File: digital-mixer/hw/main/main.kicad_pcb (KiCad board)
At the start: 2 copper layers, 114 x 112.5 mm, 184 parts, among them J1 GCT USB4085, J10 MIDI OUT SJ-43514-SMT, J2 LiPo 1S 3000 mAh (з платою за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, J3 IN1 SJ-43514-SMT, J4 IN2 SJ-43514-SMT, J5 IN3 SJ-43514-SMT, J6 IN4 SJ-43514-SMT, J7 MAIN OUT SJ-43514-SMT, J8 AUX OUT SJ-43514-SMT, J9 PHONES SJ-43514-SMT, Q1 AO3401A, SW1 Power 7x7 DPDT self-lock, SW10 EC11 ch3.1, SW11 EC11 ch3.2, SW12 EC11 ch3.3, SW13 Mute 3 TSF-1266, SW14 EC11 ch4.1, SW15 EC11 ch4.2, SW16 EC11 ch4.3, SW17 Mute 4 TSF-1266, SW18 EC11 master, SW19 FX1 TSF-1266, SW2 EC11 ch1.1, SW20 FX2 TSF-1266, SW21 AUX TSF-1266, SW22 CUE TSF-1266, SW23 SHIFT TSF-1266, SW3 EC11 ch1.2, SW4 EC11 ch1.3, SW5 Mute 1 TSF-1266, SW6 EC11 ch2.1, SW7 EC11 ch2.2, SW8 EC11 ch2.3, SW9 Mute 2 TSF-1266, U1 Teensy 4.1, U10 PCM5102A, U11 TPA6132A2, U12 MCP23017-E/SO, U13 MCP23017-E/SO, U2 USBLC6-2SC6, U3 TP4056, U4 TPS63802, U5 LP5907MFX-3.3, U6 PCM1865, U7 PCM1865, U8 PCM5102A, U9 PCM5102A

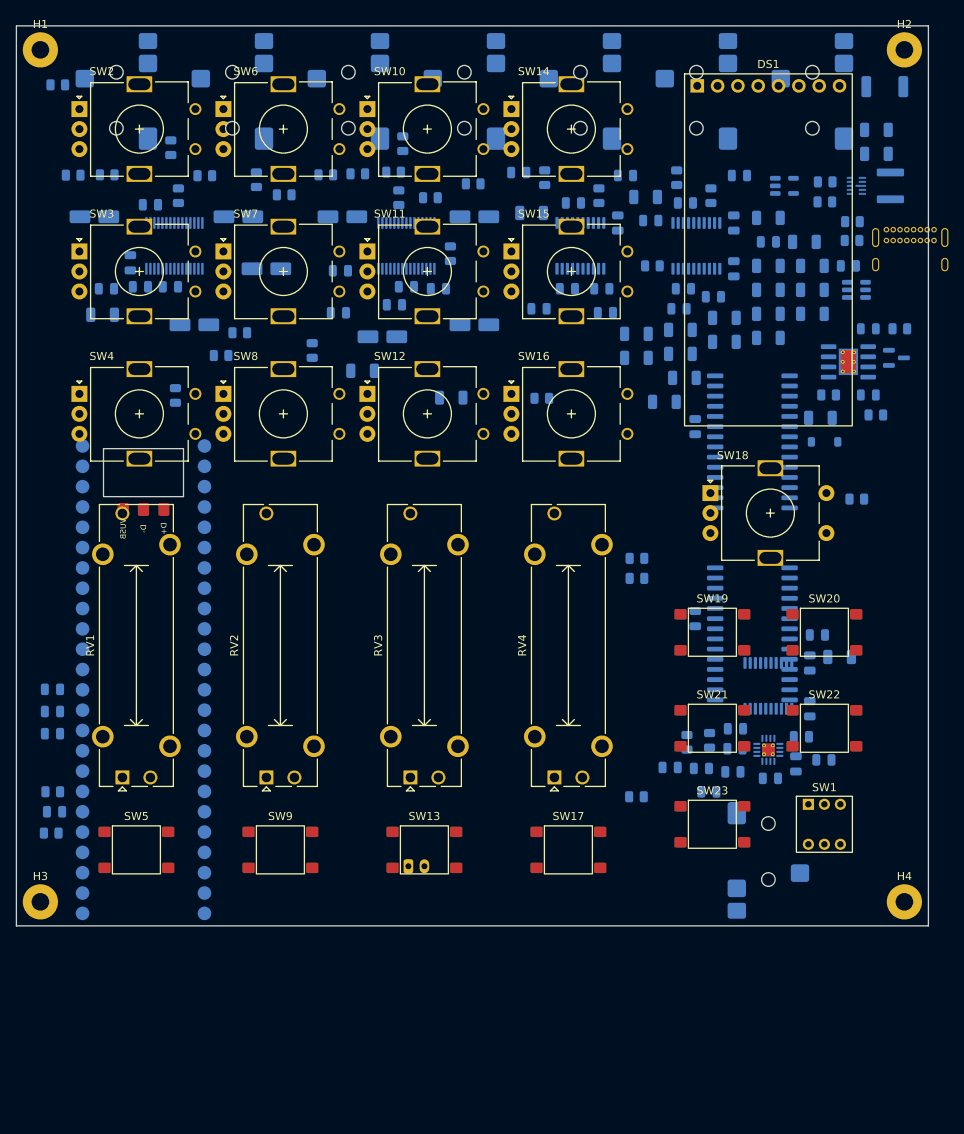
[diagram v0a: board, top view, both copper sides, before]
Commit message: digital-mixer: компоновка A (DM24), footprint за кресленнями GMT147, TSF-1266, кнопки 7x7
- розстановка: джеки ззаду, Teensy під Mute (microSD ліворуч), електроніка під правою колонкою,
  M2 у кутах; DRC розстановки: без перетинів корпусів і замикань
- route_pcb.py / fix_pcb.py для 2 шарів (з Rev A)

Co-Authored-By: Claude Opus 5.5 <noreply@anthropic.com>
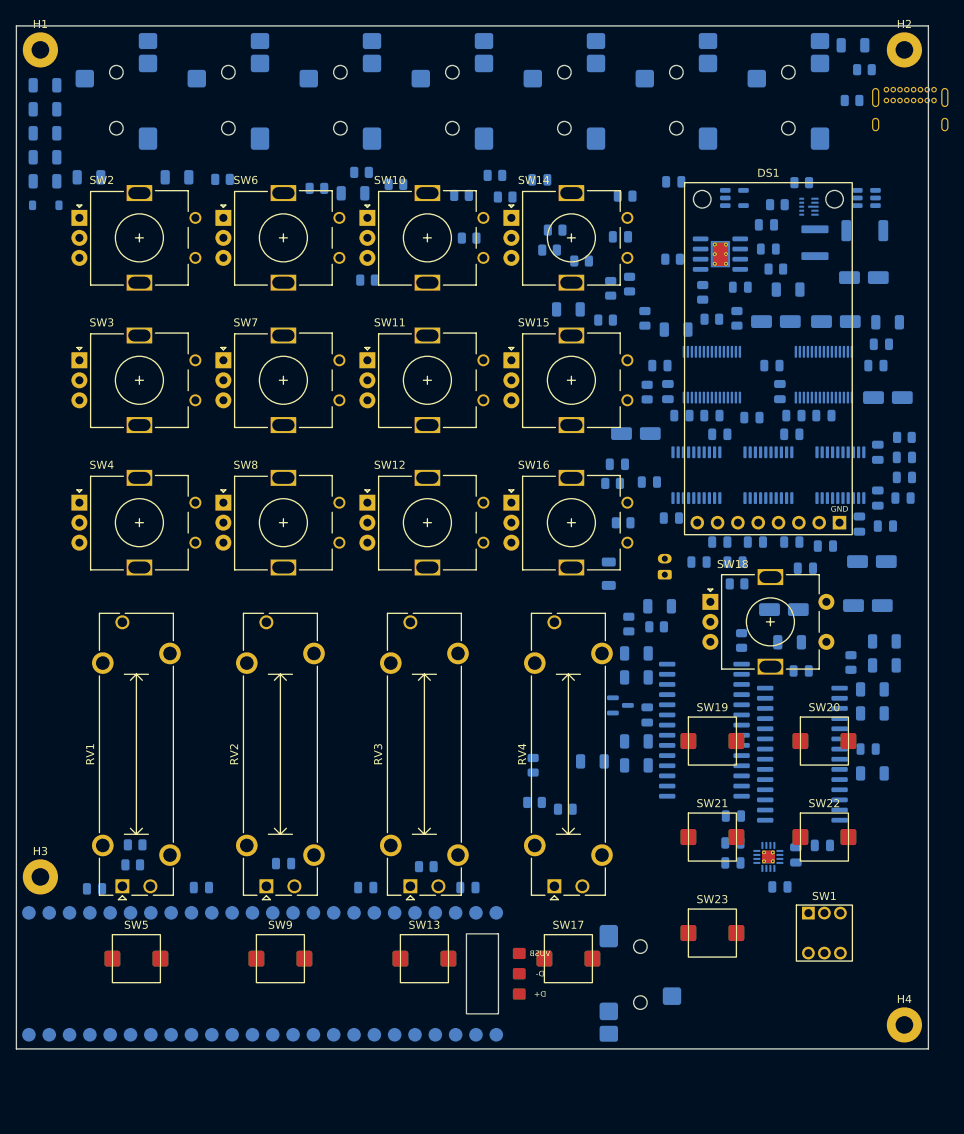
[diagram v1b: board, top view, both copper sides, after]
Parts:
- moved C80 118.2 mm to (76.4, 127.7)
- moved C64 103.9 mm to (23.6, 36.4)
- moved D3 101.7 mm to (23.7, 42.4)
- moved C15 101.7 mm to (128.9, 66.5)
- moved C7 96.2 mm to (29.1, 38.9)
- moved C6 86.7 mm to (23.6, 30.4)
- moved C53 86.2 mm to (23.6, 27.4)
- moved C81 82.2 mm to (23.6, 39.4)
- moved C16 79.8 mm to (111.9, 69.0)
- moved C63 78.1 mm to (23.6, 33.4)
- moved C27 73.9 mm to (115.9, 93.0)
- moved C12 72.7 mm to (114.9, 57.0)
- moved C20 71.7 mm to (102.5, 58.0)
- moved C14 71.5 mm to (122.4, 57.0)
- moved C19 69.9 mm to (100.4, 62.5)
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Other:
- board size 114 x 112.5 mm -> 114 x 127.9 mm

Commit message: digital-mixer: двошарова плата розведена (DRC: 0 розривів, 0 порушень по міді)
- Teensy праворуч спереду (microSD у правий торець), USB-C і PHONES на фронті: USB D+/D- ~30 мм
- блок TPS63802 за прикладом TI, доріжки зафіксовані; конденсатори біля виводів
- footprint TSF-1266 без подвійного courtyard; route_pcb зберігає зафіксовані доріжки
- docs/04-pcb.md

Co-Authored-By: Claude Opus 5.5 <noreply@anthropic.com>
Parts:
- U11: footprint Package_DFN_QFN:WQFN-16-1EP_3x3mm_P0.5mm_EP1.6x1.6mm_ThermalVias -> Package_DFN_QFN:WQFN-16-1EP_3x3mm_P0.5mm_EP1.6x1.6mm
- U3: footprint Package_SO:SOIC-8-1EP_3.9x4.9mm_P1.27mm_EP2.41x3.3mm_ThermalVias -> Package_SO:SOIC-8-1EP_3.9x4.9mm_P1.27mm_EP2.41x3.3mm
- moved J1 131.3 mm to (69.2, 141.8)
- moved R9 131.1 mm to (61.0, 139.3)
- moved R10 124.9 mm to (65.0, 139.1)
- moved U2 110.1 mm to (66.2, 133.8)
- moved C6 103.0 mm to (86.5, 111.9)
- moved C81 102.4 mm to (124.6, 22.4)
- moved C52 95.3 mm to (92.0, 111.9)
- moved C7 95.2 mm to (122.5, 57.2)
- moved C3 90.0 mm to (119.7, 128.1)
- moved R8 86.1 mm to (120.9, 125.1)
- moved C8 83.1 mm to (122.5, 49.0)
- moved R7 76.8 mm to (111.3, 128.1)
- moved C53 72.1 mm to (90.0, 55.4)
- moved C63 65.5 mm to (84.5, 57.4)
- moved C64 63.5 mm to (84.5, 54.4)
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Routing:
- net /+4V2: track 0.00 -> 5.90 mm
- net /BB_L1: track 0.00 -> 4.27 mm
- net /BB_L2: track 0.00 -> 4.23 mm
- net /VSYS: track 0.00 -> 3.35 mm

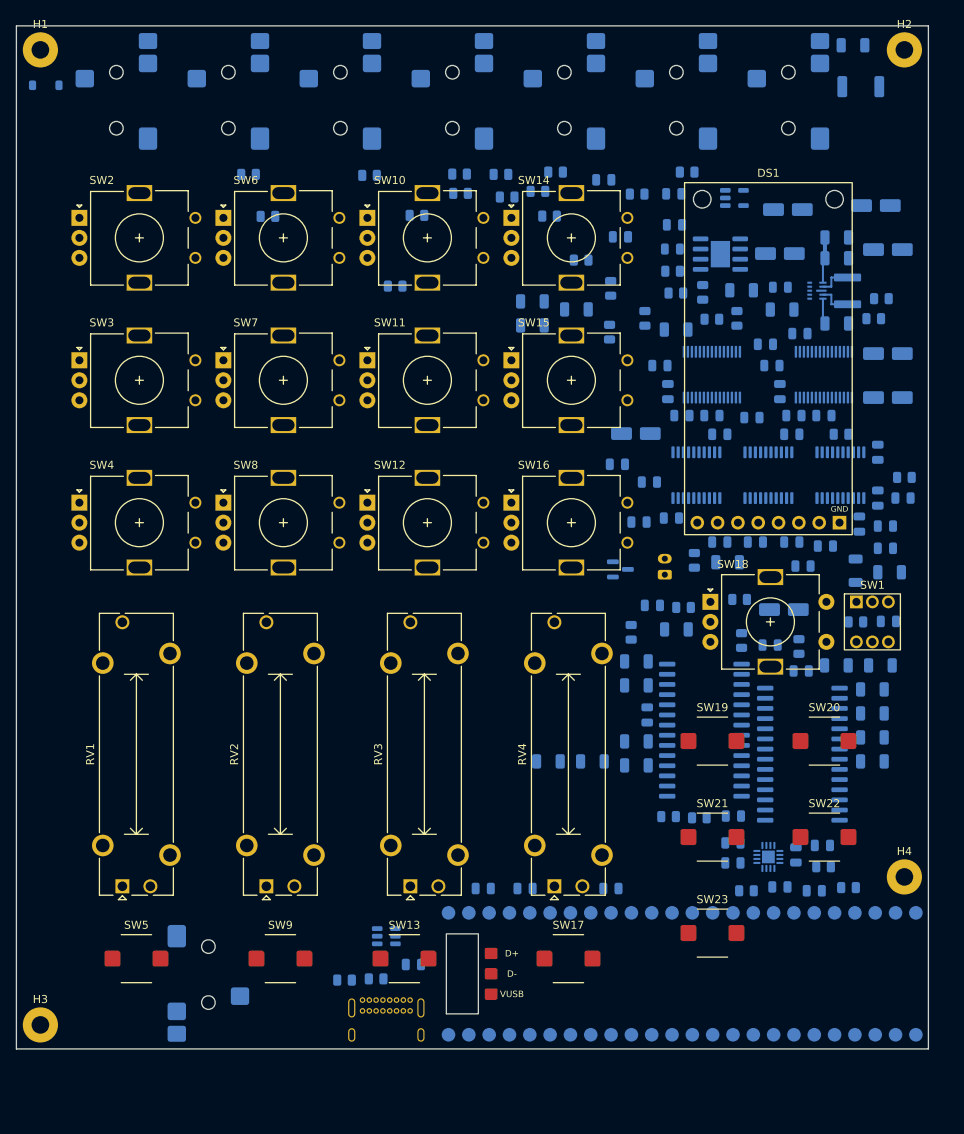
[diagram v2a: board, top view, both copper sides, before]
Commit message: digital-mixer: компоновка C (DM25-DM30), SMD-енкодери, USB4110, розводка 0 помилок
- компоновка C: колонки каналів на одних осях, ON / дисплей / MASTER в один ряд,
  Teensy у передньому правому куті, виходи на правому торці, M2 у чотирьох кутах
- EC12SY SMD з кнопками (DM26) + третій MCP23017; кнопку CUE прибрано (DM28)
- кнопка живлення 5,8 мм SMD (DM27), USB-C GCT USB4110 SMD (DM30), JST PH SMD
- 33 Ω на тактах I2S / TDM (DM29); такти 60-73 мм замість ~110
- 3D-моделі для всіх власних і стокових footprint без моделі (hw/lib/gen_3d.py)
- common: route_pcb --hole-keep, rip_near.py, параметри проєкту в kisch
- DRC: 0 порушень, 0 нез'єднаних, 0 розбіжностей зі схемою; ERC 0

Co-Authored-By: Claude Opus 5.5 <noreply@anthropic.com>
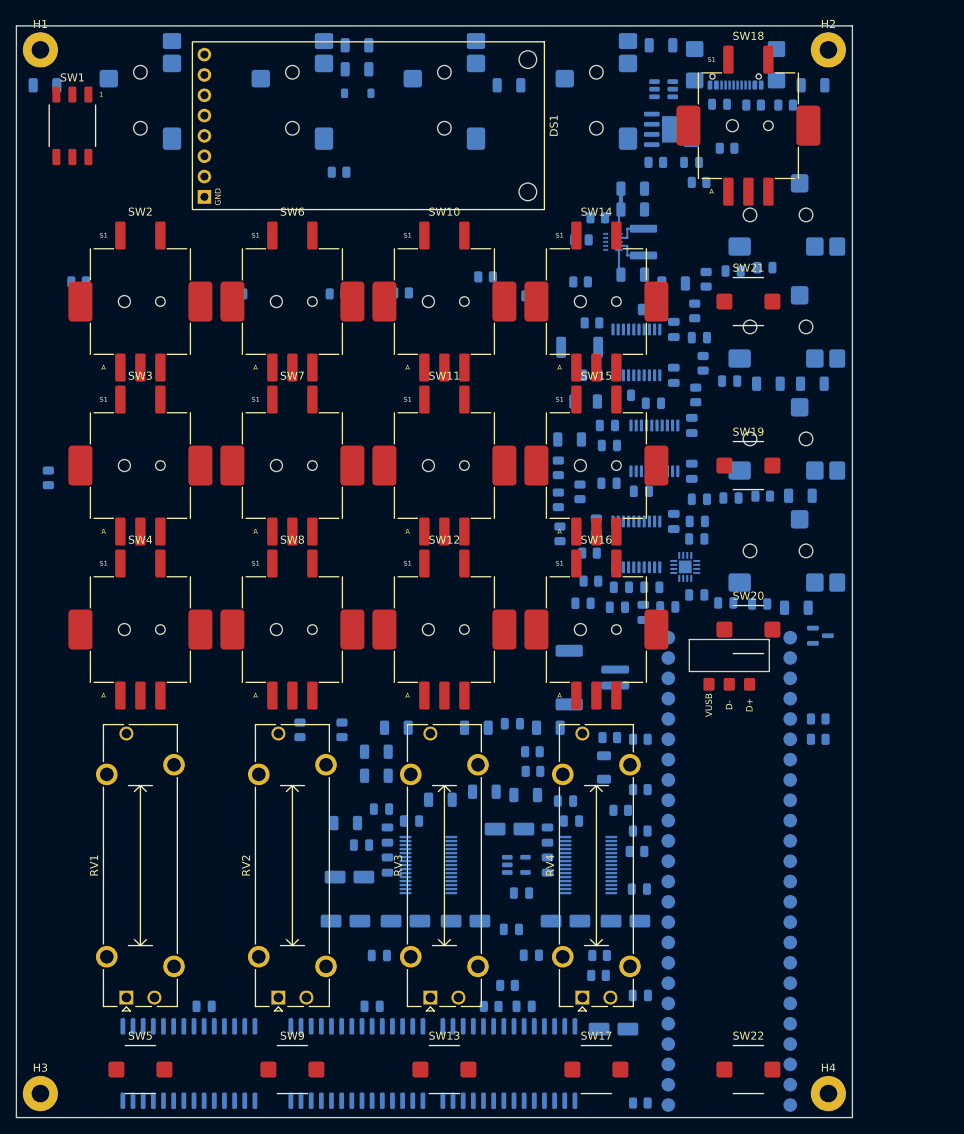
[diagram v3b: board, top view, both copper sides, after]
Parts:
- removed SW23: SHIFT TSF-1266, pocket-digital:SW_TSF-1266_6x6mm_SMD
- added C82: 10u, Capacitor_SMD:C_1206_3216Metric, B.Cu at (119.6, 27.4)
- added R44: 470, Resistor_SMD:R_0805_2012Metric, B.Cu at (105.8, 62.2)
- added R45: 470, Resistor_SMD:R_0805_2012Metric, B.Cu at (91.6, 85.9)
- added R46: 470, Resistor_SMD:R_0805_2012Metric, B.Cu at (91.8, 89.4)
- added R47: 33 0.5W, Resistor_SMD:R_2010_5025Metric, B.Cu at (90.4, 60.2)
- added R48: 10 0.25W, Resistor_SMD:R_1206_3216Metric, B.Cu at (93.4, 112.7)
- added U14: MCP23017-E/SO, Package_SO:SOIC-28W_7.5x17.9mm_P1.27mm, B.Cu at (81.6, 149.7)
- C81: value 10u -> 100n; footprint Capacitor_SMD:C_1206_3216Metric -> Capacitor_SMD:C_0805_2012Metric
- J1: value GCT USB4085 -> GCT USB4110-GF-A; footprint Connector_USB:USB_C_Receptacle_GCT_USB4085 -> Connector_USB:USB_C_Receptacle_GCT_USB4110
- J2: footprint Connector_JST:JST_PH_B2B-PH-K_1x02_P2.00mm_Vertical -> Connector_JST:JST_PH_S2B-PH-SM4-TB_1x02-1MP_P2.00mm_Horizontal
- R10: value 5.1k -> 10k
- R11: value 2.4k -> 10k
- R12, R13: value 1k -> 100k
- R14: value 100k -> 5.1k
- R15: value 665k -> 5.1k
- R16: value 91k -> 2.4k
- R17, R18: value 100k -> 1k
- R19, R23, R25, R32, R34: value 10k -> 100k
- R20: value 100k -> 665k
- R21: value 10k -> 91k
- R24, R33: value 100k -> 10k
- R26, R35: value 33 -> 10k
- R31, R7, R8: value 100k -> 33
- R36, R38: value 470 -> 100k
- R37, R39: value 470 -> 10k
- R40: value 470 -> 33
- R42: value 33 0.5W -> 470; footprint Resistor_SMD:R_2010_5025Metric -> Resistor_SMD:R_0805_2012Metric
- R43: value 10 0.25W -> 470; footprint Resistor_SMD:R_1206_3216Metric -> Resistor_SMD:R_0805_2012Metric
- R5, R6: value 10k -> 33
- R9: value 5.1k -> 33
- SW1: value Power 7x7 DPDT self-lock -> Power 5.8mm DPDT self-lock SMD; footprint pocket-digital:SW_Push_Latching_DPDT_7x7mm -> pocket-digital:SW_Push_Latching_DPDT_5.8mm_SMD
- SW10: value EC11 ch3.1 -> EC12SY ch3.1; footprint Rotary_Encoder:RotaryEncoder_Alps_EC11E_Vertical_H20mm -> pocket-digital:RotaryEncoder_EC12SY_SMD
- SW11: value EC11 ch3.2 -> EC12SY ch3.2; footprint Rotary_Encoder:RotaryEncoder_Alps_EC11E_Vertical_H20mm -> pocket-digital:RotaryEncoder_EC12SY_SMD
- SW12: value EC11 ch3.3 -> EC12SY ch3.3; footprint Rotary_Encoder:RotaryEncoder_Alps_EC11E_Vertical_H20mm -> pocket-digital:RotaryEncoder_EC12SY_SMD
- SW14: value EC11 ch4.1 -> EC12SY ch4.1; footprint Rotary_Encoder:RotaryEncoder_Alps_EC11E_Vertical_H20mm -> pocket-digital:RotaryEncoder_EC12SY_SMD
- SW15: value EC11 ch4.2 -> EC12SY ch4.2; footprint Rotary_Encoder:RotaryEncoder_Alps_EC11E_Vertical_H20mm -> pocket-digital:RotaryEncoder_EC12SY_SMD
- SW16: value EC11 ch4.3 -> EC12SY ch4.3; footprint Rotary_Encoder:RotaryEncoder_Alps_EC11E_Vertical_H20mm -> pocket-digital:RotaryEncoder_EC12SY_SMD
- SW18: value EC11 master -> EC12SY master; footprint Rotary_Encoder:RotaryEncoder_Alps_EC11E-Switch_Vertical_H20mm -> pocket-digital:RotaryEncoder_EC12SY_SMD
- SW2: value EC11 ch1.1 -> EC12SY ch1.1; footprint Rotary_Encoder:RotaryEncoder_Alps_EC11E_Vertical_H20mm -> pocket-digital:RotaryEncoder_EC12SY_SMD
- SW22: value CUE TSF-1266 -> SHIFT TSF-1266
- SW3: value EC11 ch1.2 -> EC12SY ch1.2; footprint Rotary_Encoder:RotaryEncoder_Alps_EC11E_Vertical_H20mm -> pocket-digital:RotaryEncoder_EC12SY_SMD
- SW4: value EC11 ch1.3 -> EC12SY ch1.3; footprint Rotary_Encoder:RotaryEncoder_Alps_EC11E_Vertical_H20mm -> pocket-digital:RotaryEncoder_EC12SY_SMD
- SW6: value EC11 ch2.1 -> EC12SY ch2.1; footprint Rotary_Encoder:RotaryEncoder_Alps_EC11E_Vertical_H20mm -> pocket-digital:RotaryEncoder_EC12SY_SMD
- SW7: value EC11 ch2.2 -> EC12SY ch2.2; footprint Rotary_Encoder:RotaryEncoder_Alps_EC11E_Vertical_H20mm -> pocket-digital:RotaryEncoder_EC12SY_SMD
- SW8: value EC11 ch2.3 -> EC12SY ch2.3; footprint Rotary_Encoder:RotaryEncoder_Alps_EC11E_Vertical_H20mm -> pocket-digital:RotaryEncoder_EC12SY_SMD
- moved J1 124.9 mm to (109.9, 23.7), turned to 0 degrees
- moved SW1 117.7 mm to (27.0, 32.5)
- moved U2 111.4 mm to (100.9, 27.9)
- moved C81 108.8 mm to (97.9, 127.9)
- moved J9 99.9 mm to (123.2, 85.6), turned to 180 degrees
- moved C13 94.7 mm to (61.6, 126.4)
- moved C52 94.2 mm to (62.6, 22.4)
- moved C14 94.2 mm to (61.1, 131.9)
- moved C24 93.1 mm to (88.6, 131.9)
- moved C25 91.2 mm to (96.1, 131.9)
- moved C26 90.4 mm to (81.6, 120.4)
- moved C6 89.8 mm to (62.6, 25.4)
- moved C15 88.4 mm to (76.1, 131.9)
- moved U5 87.7 mm to (82.5, 124.9)
- moved R13 83.3 mm to (92.9, 136.2)
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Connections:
- C77 pad 1: /FADER1 -> /+3V3
- C78 pad 1: /FADER2 -> /FADER1
- C79 pad 1: /FADER3 -> /FADER2
- C80 pad 1: /FADER4 -> /FADER3
- C81 pad 1: /+3V3 -> /FADER4
- R10 pad 1: /CC2 -> /DAC_XSMT
- R11 pad 1: /CHG_PROG -> /HP_EN
- R12 pad 1: /VBUS -> /VSYS
- R12 pad 2: /CHG_LED_RA -> /VBAT_SENSE
- R13 pad 1: /VBUS -> /VBAT_SENSE
- R13 pad 2: /CHG_LED_GA -> /GND
- R14 pad 1: /VBUS -> /CC1
- R15 pad 1: /+4V2 -> /CC2
- R15 pad 2: /BB_FB -> /GND
- R16 pad 1: /BB_FB -> /CHG_PROG
- R17 pad 1: /PWR_EN -> /VBUS
- R17 pad 2: /GND -> /CHG_LED_RA
- R18 pad 1: /IN1_T -> /VBUS
- R18 pad 2: /GND -> /CHG_LED_GA
- R19 pad 1: /IN1_T -> /VBUS
- R19 pad 2: /IN1_LS -> /GND
- R20 pad 1: /IN1_R -> /+4V2
- R20 pad 2: /GND -> /BB_FB
- R21 pad 1: /IN1_R -> /BB_FB
- R21 pad 2: /IN1_RS -> /GND
- R22 pad 1: /IN2_T -> /PWR_EN
- R23 pad 1: /IN2_T -> /IN1_T
- R23 pad 2: /IN2_LS -> /GND
- R24 pad 1: /IN2_R -> /IN1_T
- R24 pad 2: /GND -> /IN1_LS
- R25 pad 1: /IN2_R -> /IN1_R
- R25 pad 2: /IN2_RS -> /GND
- R26 pad 1: /ADC1_DOUT -> /IN1_R
- R26 pad 2: /ADC_DOUT -> /IN1_RS
- R27 pad 1: /IN3_T -> /IN2_T
- R28 pad 1: /IN3_T -> /IN2_T
- R28 pad 2: /IN3_LS -> /IN2_LS
- R29 pad 1: /IN3_R -> /IN2_R
- R30 pad 1: /IN3_R -> /IN2_R
- R30 pad 2: /IN3_RS -> /IN2_RS
- R31 pad 1: /IN4_T -> /ADC1_DOUT
- R31 pad 2: /GND -> /ADC_DOUT
- R32 pad 1: /IN4_T -> /IN3_T
- R32 pad 2: /IN4_LS -> /GND
- R33 pad 1: /IN4_R -> /IN3_T
- R33 pad 2: /GND -> /IN3_LS
- R34 pad 1: /IN4_R -> /IN3_R
- R34 pad 2: /IN4_RS -> /GND
- R35 pad 1: /ADC2_DOUT -> /IN3_R
- R35 pad 2: /ADC_DOUT -> /IN3_RS
- R36 pad 1: /MAIN_OL -> /IN4_T
- R36 pad 2: /MAIN_L -> /GND
- R37 pad 1: /MAIN_OR -> /IN4_T
- R37 pad 2: /MAIN_R -> /IN4_LS
- R38 pad 1: /AUX_OL -> /IN4_R
- R38 pad 2: /AUX_L -> /GND
- R39 pad 1: /AUX_OR -> /IN4_R
- R39 pad 2: /AUX_R -> /IN4_RS
- R40 pad 1: /CUE_OL -> /ADC2_DOUT
- R40 pad 2: /CUE_L -> /ADC_DOUT
- R41 pad 1: /CUE_OR -> /MAIN_OL
- R41 pad 2: /CUE_R -> /MAIN_L
- R42 pad 1: /+3V3 -> /MAIN_OR
- R42 pad 2: /MIDI_SRC -> /MAIN_R
- R43 pad 1: /MIDI_TX -> /AUX_OL
- R43 pad 2: /MIDI_SINK -> /AUX_L
- R5 pad 1: /DAC_XSMT -> /DAC_BCK_T
- R5 pad 2: /GND -> /DAC_BCK
- R6 pad 1: /HP_EN -> /DAC_LRCK_T
- R6 pad 2: /GND -> /DAC_LRCK
- R7 pad 1: /VSYS -> /ADC_BCK_T
- R7 pad 2: /VBAT_SENSE -> /ADC_BCK
- R8 pad 1: /VBAT_SENSE -> /ADC_LRCK_T
- R8 pad 2: /GND -> /ADC_LRCK
- R9 pad 1: /CC1 -> /ADC_MCLK_T
- R9 pad 2: /GND -> /ADC_MCLK
- SW1 pad 1: /VSYS -> /GND
- SW1 pad 3: /GND -> /VSYS
- SW10 pad MP: (no net) -> /GND
- SW11 pad MP: (no net) -> /GND
- SW12 pad MP: (no net) -> /GND
- SW14 pad MP: (no net) -> /GND
- SW15 pad MP: (no net) -> /GND
- SW16 pad MP: (no net) -> /GND
- SW18 pad MP: (no net) -> /GND
- SW2 pad MP: (no net) -> /GND
- SW22 pad 1: /BTN_CUE -> /BTN_SHIFT
- SW3 pad MP: (no net) -> /GND
- SW4 pad MP: (no net) -> /GND
- SW6 pad MP: (no net) -> /GND
- SW7 pad MP: (no net) -> /GND
- SW8 pad MP: (no net) -> /GND
- U1 pad 25: /ADC_MCLK -> /ADC_MCLK_T
- U1 pad 42: /DAC_LRCK -> /DAC_LRCK_T
- U1 pad 43: /DAC_BCK -> /DAC_BCK_T
- U1 pad 44: unconnected-(U1-22_A8_CTX1-Pad44) -> /MCP3_INT
- U1 pad 5: /ADC_LRCK -> /ADC_LRCK_T
- U1 pad 6: /ADC_BCK -> /ADC_BCK_T
- U12 pad 28: /BTN_FX1 -> unconnected-(U12-GPA7-Pad28)
- U12 pad 8: /BTN_FX2 -> unconnected-(U12-GPB7-Pad8)
- U13 pad 28: /BTN_AUX -> unconnected-(U13-GPA7-Pad28)
- U13 pad 8: /BTN_CUE -> unconnected-(U13-GPB7-Pad8)
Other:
- board size 114 x 127.9 mm -> 104.5 x 136.5 mm

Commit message: digital-mixer: 4 шари (DM31), пара USB D+/D- наперед, розводка 0 помилок
- плата 4 шари як Rev A: F сигнали / In1 GND / In2 сигнали й живлення / B сигнали; доріжки 0,2 мм
- USB D+/D- прокладено парою 0,2/0,2 мм над In1 (92,5 / 90,9 мм) і зафіксовано до автороутера
- кнопки правої колонки повернуті площадкою GND до пари; конденсатори накачки й вихідні
  470 Ом ЦАП, конденсатори TPA6132A2 - біля виводів; TPA6132A2 розвернута до PHONES
- common: patch_route --ignore, fix_pcb --no-cleanup і переходи в острівці GND, кінці доріжок у
  переходах не вважаються висячими, виправлено падіння на видалених переходах
- DRC: 0 порушень, 0 нез'єднаних, 0 розбіжностей зі схемою; ERC 0

Co-Authored-By: Claude Opus 5.5 <noreply@anthropic.com>
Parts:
- moved C42 71.3 mm to (65.0, 110.7)
- moved C41 70.2 mm to (118.0, 64.7)
- moved C35 63.3 mm to (67.5, 107.7)
- moved C23 54.1 mm to (118.0, 78.7)
- moved Q1 44.9 mm to (89.0, 64.2)
- moved C11 41.8 mm to (89.5, 67.7)
- moved C18 39.5 mm to (81.0, 107.7)
- moved R10 27.3 mm to (88.8, 90.8)
- moved C66 24.5 mm to (112.7, 78.5)
- moved R44 20.6 mm to (92.5, 77.9)
- moved C10 20.0 mm to (98.0, 95.2)
- moved C68 19.8 mm to (93.1, 92.6)
- moved C55 17.6 mm to (108.7, 64.7)
- moved R41 16.6 mm to (93.2, 67.4)
- moved R42 15.8 mm to (92.8, 59.9)
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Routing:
- net /USB_DP: track 0.00 -> 92.5 mm, vias 0 -> 1
- net /USB_DN: track 0.00 -> 90.9 mm, vias 0 -> 1

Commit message: digital-mixer: Teensy на гребінках з PSRAM (DM35), прошивка 0.2, GPL-3.0 (DM36)
Плата: Teensy 4.1 на гребінках у наскрізні отвори (зазор 2,5 мм під PSRAM),
D-/D+ теж наскрізні, Teensy за 6 мм від переднього краю, бокові джеки з кроком
12,5 мм, лапки EC12SY укорочено; перерозведено - DRC 0 порушень, 0 розривів.
Gerber, BOM і файли NextPCB оновлено.

Прошивка: метри каналів після фейдера (CLIP - лише вхід АЦП), калібрування
фейдерів, SHIFT HOLD/TOGGLE, MASTER = AUX у шарі AUX, кроки гучностей,
виправлено EQ на мінімумі, піктограма батареї, назви FX на екрані; збірка
uac2 (UAC2 8x8, 48 kHz) через tools/setup_uac2.sh.

Ліцензія digital-mixer/ - GPL-3.0-or-later.

Co-Authored-By: Claude Opus 5.5 <noreply@anthropic.com>
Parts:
- U1: footprint pocket-digital:Teensy41_SMD -> pocket-digital:Teensy41_THT
- moved C42 95.2 mm to (100.6, 22.4)
- moved C5 88.3 mm to (62.6, 25.4)
- moved C41 69.7 mm to (62.6, 22.4)
- moved C23 58.2 mm to (67.5, 107.7)
- moved C64 58.1 mm to (23.6, 30.4)
- moved D3 58.0 mm to (120.7, 30.4)
- moved C6 57.0 mm to (119.6, 27.4)
- moved Q1 45.3 mm to (120.5, 96.7)
- moved C2 44.8 mm to (79.0, 115.7)
- moved C11 43.4 mm to (84.0, 110.7)
- moved C52 39.3 mm to (23.6, 27.4)
- moved C66 39.2 mm to (86.9, 108.0)
- moved C63 39.0 mm to (62.6, 28.4)
- moved C82 38.1 mm to (81.6, 30.4)
- moved R10 31.6 mm to (120.3, 93.5)
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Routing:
- net /USB_DP: track 92.5 -> 63.3 mm
- net /USB_DN: track 90.9 -> 65.4 mm
